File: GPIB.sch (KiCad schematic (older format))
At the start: 22 parts

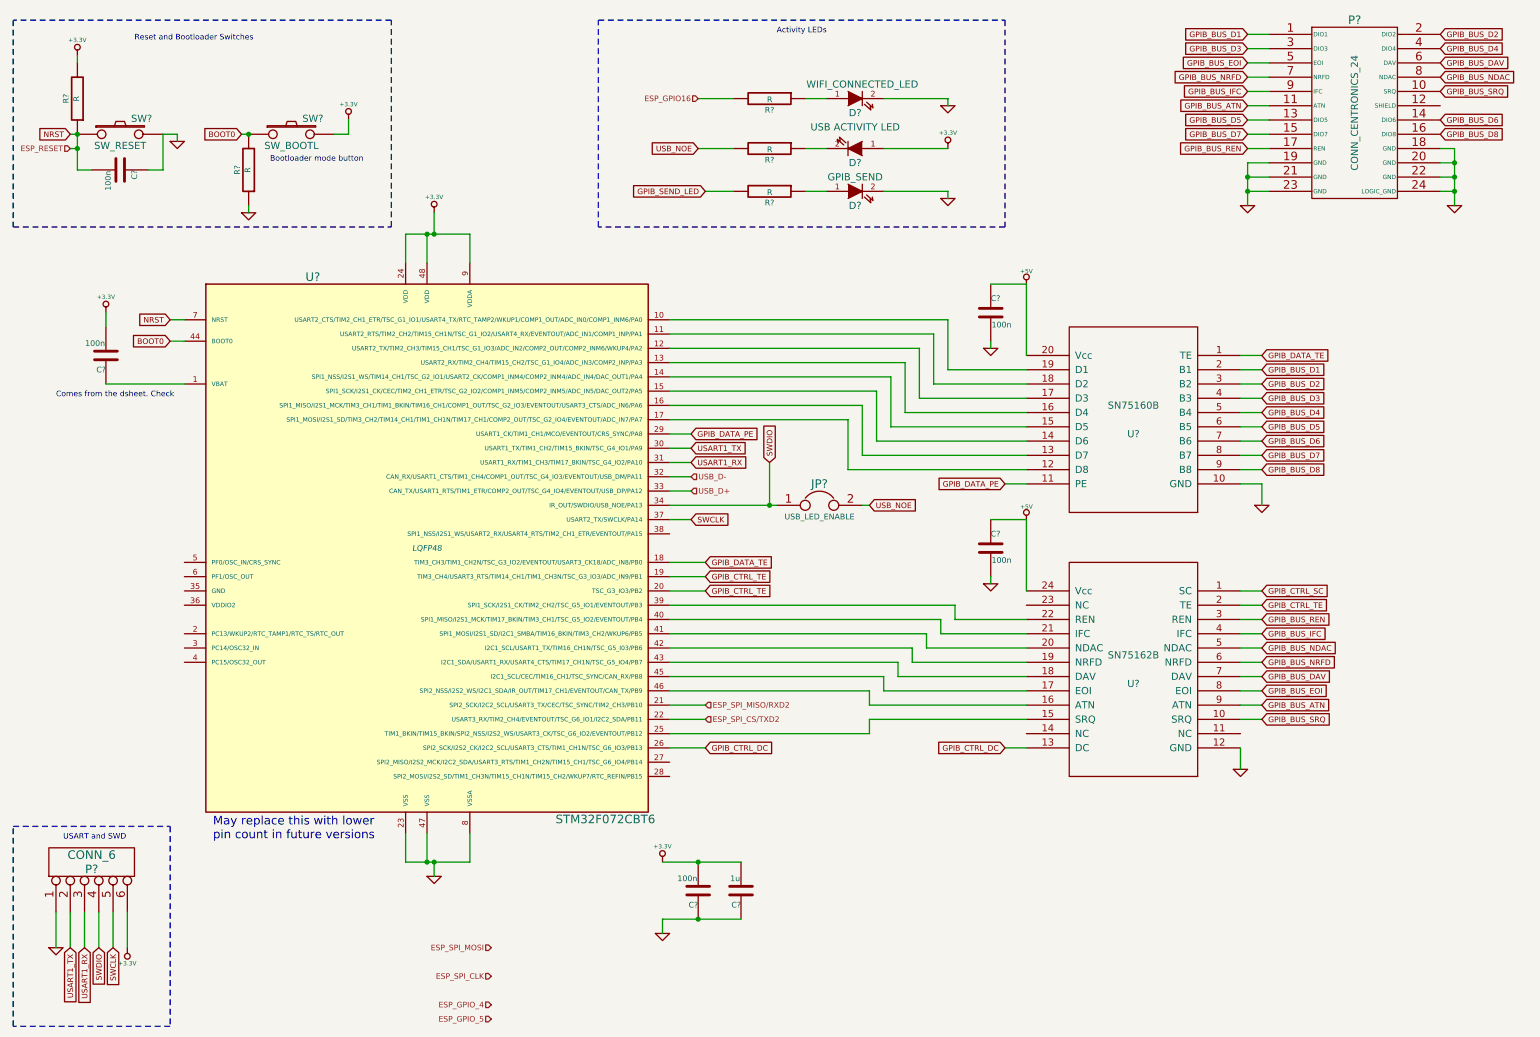
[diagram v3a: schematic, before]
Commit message: ESP doesn't seem to support UART2, switch to UART1
As far as I can tell the TXD2, RXD2 ports are not documented
If they do work, they will only work exclusively of TX1/RX1.
So better to just use the main UART.
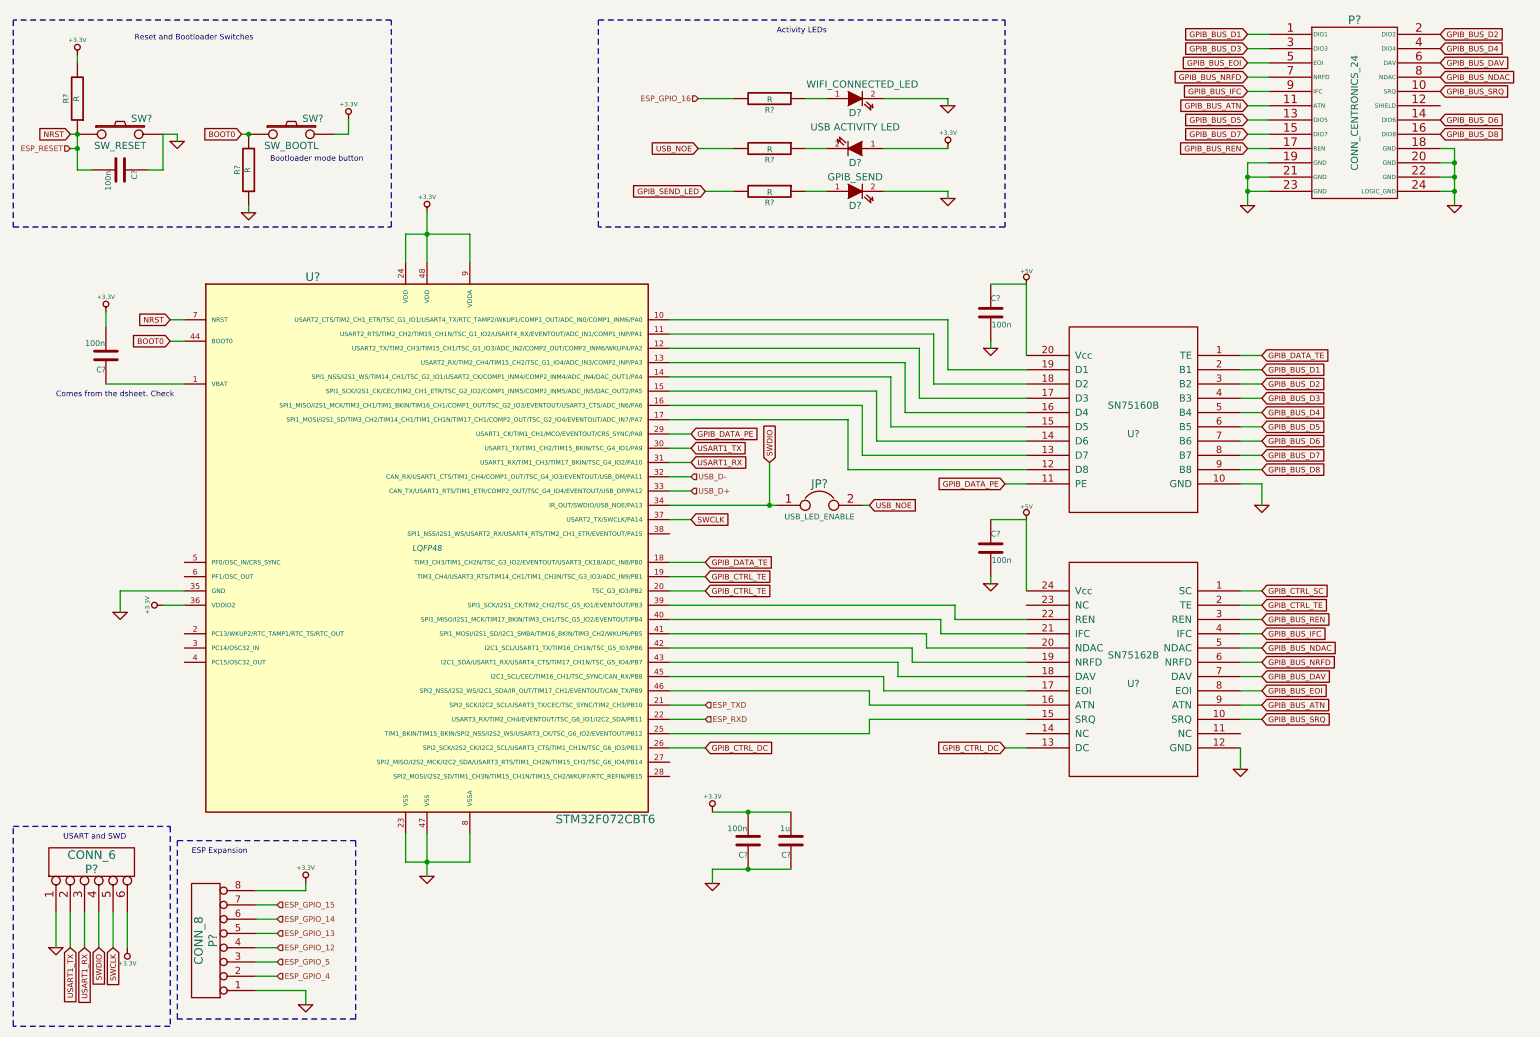
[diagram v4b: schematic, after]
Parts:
- added P?: CONN_8, symbol CONN_8
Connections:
- net +3.3V: now also U?.36 (VDDIO2), P?.8 (P8)
- net ESP_GPIO_4: now also P?.2 (P2)
- net ESP_GPIO_5: now also P?.3 (P3)
- net GND: now also U?.35 (GND), P?.1 (P1)
- net ESP_GPIO16 renamed ESP_GPIO_16
- net ESP_SPI_CS/TXD2 renamed ESP_RXD
- net ESP_SPI_MISO/RXD2 renamed ESP_TXD
- new net ESP_GPIO_12: P?.4 (P4)
- new net ESP_GPIO_13: P?.5 (P5)
- new net ESP_GPIO_14: P?.6 (P6)
- new net ESP_GPIO_15: P?.7 (P7)
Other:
- note added: "ESP Expansion\n"
- note removed: "May replace this with lower\npin count in future versions"
- moved on the sheet: C?
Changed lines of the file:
@@
 	1    0    0    -1
 $EndComp
-Text Notes 2050 6400 0    60   ~ 0
-May replace this with lower\npin count in future versions
 $Comp
 L STM32F072CBT6 U?
@@
 $EndComp
 Wire Wire Line
-	5250 4050 5950 4050
-Wire Wire Line
-	5950 4050 6000 4050
+	5250 4050 6000 4050
 Wire Wire Line
 	5250 3950 5400 3950
@@
 	10650 1550 10750 1550
 Wire Wire Line
-	10750 1550 10750 1650
-Wire Wire Line
-	10750 1650 10750 1750
-Wire Wire Line
-	10750 1750 10750 1850
-Wire Wire Line
-	10750 1850 10750 1950
+	10750 1550 10750 1950
 Wire Wire Line
 	10650 1850 10750 1850
@@
 $EndComp
 Wire Wire Line
-	9300 1650 9300 1750
-Wire Wire Line
-	9300 1750 9300 1850
-Wire Wire Line
-	9300 1850 9300 1950
+	9300 1650 9300 1950
 Connection ~ 9300 1750
 Connection ~ 9300 1850
@@
 Connection ~ 1100 1450
 Wire Wire Line
-	1100 1450 1100 1550
-Wire Wire Line
-	1100 1550 1100 1700
+	1100 1450 1100 1700
 Wire Wire Line
 	1100 1700 1200 1700
@@
 Wire Wire Line
 	1300 3200 1850 3200
-Text HLabel 5500 5550 2    39   Input ~ 0
-ESP_SPI_CS/TXD2
-Text HLabel 4000 7150 0    39   Input ~ 0
-ESP_SPI_MOSI
-Text HLabel 5500 5450 2    39   Input ~ 0
-ESP_SPI_MISO/RXD2
-Text HLabel 4000 7350 0    39   Input ~ 0
-ESP_SPI_CLK
-Text HLabel 4000 7550 0    39   Input ~ 0
+Text HLabel 2500 7350 2    39   Input ~ 0
 ESP_GPIO_4
-Text HLabel 4000 7650 0    39   Input ~ 0
+Text HLabel 2500 7250 2    39   Input ~ 0
 ESP_GPIO_5
 Wire Wire Line
@@
 L +3.3V #PWR?
 U 1 1 556A2965
-P 3600 2000
-F 0 "#PWR?" H 3600 1960 30  0001 C CNN
-F 1 "+3.3V" H 3600 2110 30  0000 C CNN
-F 2 "" H 3600 2000 60  0000 C CNN
-F 3 "" H 3600 2000 60  0000 C CNN
-	1    3600 2000
+P 3550 2000
+F 0 "#PWR?" H 3550 1960 30  0001 C CNN
+F 1 "+3.3V" H 3550 2110 30  0000 C CNN
+F 2 "" H 3550 2000 60  0000 C CNN
+F 3 "" H 3550 2000 60  0000 C CNN
+	1    3550 2000
 	1    0    0    -1
 $EndComp
@@
 	3400 2350 3400 2150
 Wire Wire Line
-	3400 2150 3550 2150
-Wire Wire Line
-	3550 2150 3600 2150
-Wire Wire Line
-	3600 2150 3850 2150
-Wire Wire Line
-	3600 2150 3600 2000
+	3400 2150 3850 2150
+Wire Wire Line
+	3550 2000 3550 2350
 Wire Wire Line
 	3850 2150 3850 2350
-Connection ~ 3600 2150
-Wire Wire Line
-	3550 2350 3550 2150
 Connection ~ 3550 2150
 $Comp
 L +3.3V #PWR?
 U 1 1 556A2C71
-P 5200 6550
-F 0 "#PWR?" H 5200 6510 30  0001 C CNN
-F 1 "+3.3V" H 5200 6660 30  0000 C CNN
-F 2 "" H 5200 6550 60  0000 C CNN
-F 3 "" H 5200 6550 60  0000 C CNN
-	1    5200 6550
+P 5550 6200
+F 0 "#PWR?" H 5550 6160 30  0001 C CNN
+F 1 "+3.3V" H 5550 6310 30  0000 C CNN
+F 2 "" H 5550 6200 60  0000 C CNN
+F 3 "" H 5550 6200 60  0000 C CNN
+	1    5550 6200
 	1    0    0    -1
 $EndComp
@@
 L C C?
 U 1 1 556A2CAC
-P 5450 6750
-F 0 "C?" H 5450 6850 40  0000 L CNN
-F 1 "100n" H 5456 6665 40  0000 L CNN
-F 2 "" H 5488 6600 30  0000 C CNN
-F 3 "" H 5450 6750 60  0000 C CNN
-	1    5450 6750
+P 5800 6400
+F 0 "C?" H 5800 6500 40  0000 L CNN
+F 1 "100n" H 5806 6315 40  0000 L CNN
+F 2 "" H 5838 6250 30  0000 C CNN
+F 3 "" H 5800 6400 60  0000 C CNN
+	1    5800 6400
 	-1   0    0    1
 $EndComp
@@
 L GND #PWR?
 U 1 1 556A2E45
-P 5200 7050
-F 0 "#PWR?" H 5200 7050 30  0001 C CNN
-F 1 "GND" H 5200 6980 30  0001 C CNN
-F 2 "" H 5200 7050 60  0000 C CNN
-F 3 "" H 5200 7050 60  0000 C CNN
-	1    5200 7050
+P 5550 6700
+F 0 "#PWR?" H 5550 6700 30  0001 C CNN
+F 1 "GND" H 5550 6630 30  0001 C CNN
+F 2 "" H 5550 6700 60  0000 C CNN
+F 3 "" H 5550 6700 60  0000 C CNN
+	1    5550 6700
 	1    0    0    -1
 $EndComp
@@
 L C C?
 U 1 1 556A2E72
-P 5750 6750
-F 0 "C?" H 5750 6850 40  0000 L CNN
-F 1 "1u" H 5756 6665 40  0000 L CNN
-F 2 "" H 5788 6600 30  0000 C CNN
-F 3 "" H 5750 6750 60  0000 C CNN
-	1    5750 6750
+P 6100 6400
+F 0 "C?" H 6100 6500 40  0000 L CNN
+F 1 "1u" H 6106 6315 40  0000 L CNN
+F 2 "" H 6138 6250 30  0000 C CNN
+F 3 "" H 6100 6400 60  0000 C CNN
+	1    6100 6400
 	-1   0    0    1
 $EndComp
 Wire Wire Line
-	5200 7050 5200 6950
-Wire Wire Line
-	5200 6950 5450 6950
-Wire Wire Line
-	5450 6950 5750 6950
-Connection ~ 5450 6950
-Wire Wire Line
-	5200 6550 5450 6550
-Wire Wire Line
-	5450 6550 5750 6550
-Connection ~ 5450 6550
+	5550 6700 5550 6600
+Wire Wire Line
+	5550 6600 6100 6600
+Connection ~ 5800 6600
+Wire Wire Line
+	5550 6200 6100 6200
+Connection ~ 5800 6200
 $Comp
 L GND #PWR?
 U 1 1 556A335E
-P 3600 6650
-F 0 "#PWR?" H 3600 6650 30  0001 C CNN
-F 1 "GND" H 3600 6580 30  0001 C CNN
-F 2 "" H 3600 6650 60  0000 C CNN
-F 3 "" H 3600 6650 60  0000 C CNN
-	1    3600 6650
+P 3550 6650
+F 0 "#PWR?" H 3550 6650 30  0001 C CNN
+F 1 "GND" H 3550 6580 30  0001 C CNN
+F 2 "" H 3550 6650 60  0000 C CNN
+F 3 "" H 3550 6650 60  0000 C CNN
+	1    3550 6650
 	1    0    0    -1
 $EndComp
@@
 	3400 6350 3400 6550
 Wire Wire Line
-	3400 6550 3550 6550
-Wire Wire Line
-	3550 6550 3600 6550
-Wire Wire Line
-	3600 6550 3850 6550
-Wire Wire Line
-	3600 6550 3600 6650
+	3400 6550 3850 6550
+Wire Wire Line
+	3550 6350 3550 6650
 Wire Wire Line
 	3850 6550 3850 6350
-Connection ~ 3600 6550
-Wire Wire Line
-	3550 6350 3550 6550
 Connection ~ 3550 6550
 $Comp
@@
 	7200 1200 7200 1250
 Text HLabel 5450 1200 0    39   Input ~ 0
-ESP_GPIO16
+ESP_GPIO_16
 Wire Wire Line
 	5250 5450 5500 5450
@@
 Wire Wire Line
 	5250 5750 5500 5750
+Text HLabel 2500 7150 2    39   Input ~ 0
+ESP_GPIO_12
+Text HLabel 2500 7050 2    39   Input ~ 0
+ESP_GPIO_13
+Text HLabel 2500 6950 2    39   Input ~ 0
+ESP_GPIO_14
+Text HLabel 2500 6850 2    39   Input ~ 0
+ESP_GPIO_15
+Text HLabel 5500 5450 2    39   Input ~ 0
+ESP_TXD
+Text HLabel 5500 5550 2    39   Input ~ 0
+ESP_RXD
+Wire Wire Line
+	1400 4650 1850 4650
+Wire Wire Line
+	1850 4750 1700 4750
+$Comp
+L GND #PWR?
+U 1 1 556BAB4A
+P 1400 4800
+F 0 "#PWR?" H 1400 4800 30  0001 C CNN
+F 1 "GND" H 1400 4730 30  0001 C CNN
+F 2 "" H 1400 4800 60  0000 C CNN
+F 3 "" H 1400 4800 60  0000 C CNN
+	1    1400 4800
+	1    0    0    -1
+$EndComp
+$Comp
+L +3.3V #PWR?
+U 1 1 556BADA7
+P 1700 4750
+F 0 "#PWR?" H 1700 4710 30  0001 C CNN
+F 1 "+3.3V" H 1700 4860 30  0000 C CNN
+F 2 "" H 1700 4750 60  0000 C CNN
+F 3 "" H 1700 4750 60  0000 C CNN
+	1    1700 4750
+	0    -1   -1   0
+$EndComp
+Wire Wire Line
+	1400 4650 1400 4800
+$Comp
+L CONN_8 P?
+U 1 1 556BB559
+P 2000 7100
+F 0 "P?" V 1950 7100 60  0000 C CNN
+F 1 "CONN_8" V 2050 7100 60  0000 C CNN
+F 2 "" H 2000 7100 60  0000 C CNN
+F 3 "" H 2000 7100 60  0000 C CNN
+	1    2000 7100
+	-1   0    0    1
+$EndComp
+Wire Wire Line
+	2350 7450 2700 7450
+Wire Wire Line
+	2350 7350 2500 7350
+Wire Wire Line
+	2350 7250 2500 7250
+Wire Wire Line
+	2350 7150 2500 7150
+Wire Wire Line
+	2350 7050 2500 7050
+Wire Wire Line
+	2350 6950 2500 6950
+Wire Wire Line
+	2350 6850 2500 6850
+$Comp
+L GND #PWR?
+U 1 1 556BBE46
+P 2700 7550
+F 0 "#PWR?" H 2700 7550 30  0001 C CNN
+F 1 "GND" H 2700 7480 30  0001 C CNN
+F 2 "" H 2700 7550 60  0000 C CNN
+F 3 "" H 2700 7550 60  0000 C CNN
+	1    2700 7550
+	1    0    0    -1
+$EndComp
+$Comp
+L +3.3V #PWR?
+U 1 1 556BBE7F
+P 2700 6700
+F 0 "#PWR?" H 2700 6660 30  0001 C CNN
+F 1 "+3.3V" H 2700 6810 30  0000 C CNN
+F 2 "" H 2700 6700 60  0000 C CNN
+F 3 "" H 2700 6700 60  0000 C CNN
+	1    2700 6700
+	1    0    0    -1
+$EndComp
+Wire Wire Line
+	2350 6750 2700 6750
+Wire Wire Line
+	2700 6750 2700 6700
+Wire Wire Line
+	2700 7450 2700 7550
+Wire Notes Line
+	1800 6400 3050 6400
+Wire Notes Line
+	3050 6400 3050 7650
+Wire Notes Line
+	3050 7650 1800 7650
+Wire Notes Line
+	1800 7650 1800 6400
+Text Notes 1900 6500 0    39   ~ 0
+ESP Expansion\n
 $EndSCHEMATC

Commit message: Add rst to debug conn
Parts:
- removed P?: CONN_6, symbol CONN_6
- added P?: CONN_8, symbol CONN_8
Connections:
- net +3.3V: now also P?.8 (P8)
- net GND: now also P?.1 (P1)
- net NRST: now also P?.6 (P6)
- net SWCLK: now also P?.5 (P5)
- net SWDIO: now also P?.4 (P4)
- net USART1_RX: now also P?.3 (P3)
- net USART1_TX: now also P?.2 (P2)
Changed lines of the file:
@@
 	5250 3750 5400 3750
-$Comp
-L CONN_6 P?
-U 1 1 556A65EF
-P 1200 6550
-F 0 "P?" V 1150 6550 60  0000 C CNN
-F 1 "CONN_6" V 1250 6550 60  0000 C CNN
-F 2 "" H 1200 6550 60  0000 C CNN
-F 3 "" H 1200 6550 60  0000 C CNN
-	1    1200 6550
-	0    -1   -1   0
-$EndComp
 $Comp
 L GND #PWR?
@@
 L +3.3V #PWR?
 U 1 1 556A68A8
-P 1450 7150
-F 0 "#PWR?" H 1450 7110 30  0001 C CNN
-F 1 "+3.3V" H 1450 7260 30  0000 C CNN
-F 2 "" H 1450 7150 60  0000 C CNN
-F 3 "" H 1450 7150 60  0000 C CNN
-	1    1450 7150
+P 1650 7150
+F 0 "#PWR?" H 1650 7110 30  0001 C CNN
+F 1 "+3.3V" H 1650 7260 30  0000 C CNN
+F 2 "" H 1650 7150 60  0000 C CNN
+F 3 "" H 1650 7150 60  0000 C CNN
+	1    1650 7150
 	-1   0    0    1
 $EndComp
 Wire Wire Line
 	950  6900 950  7150
-Wire Wire Line
-	1450 6900 1450 7150
 Wire Wire Line
 	1050 6900 1050 7150
@@
 Text Notes 1900 6500 0    39   ~ 0
 ESP Expansion\n
+$Comp
+L CONN_8 P?
+U 1 1 556BDE74
+P 1300 6550
+F 0 "P?" V 1250 6550 60  0000 C CNN
+F 1 "CONN_8" V 1350 6550 60  0000 C CNN
+F 2 "" H 1300 6550 60  0000 C CNN
+F 3 "" H 1300 6550 60  0000 C CNN
+	1    1300 6550
+	0    -1   -1   0
+$EndComp
+Wire Wire Line
+	1650 6900 1650 7150
+Wire Wire Line
+	1450 6900 1450 7150
+Text GLabel 1450 7150 3    39   Input ~ 0
+NRST
 $EndSCHEMATC

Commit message: Use ST-Link (standard?) header
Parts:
- removed P?: CONN_8, symbol CONN_8
- added P?: CONN_6, symbol CONN_6
- added P?: CONN_2, symbol CONN_2
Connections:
- net +3.3V: now also P?.1
- net GND: now also P?.3
- net NRST: now also P?.5
- net SWCLK: now also P?.2
- net SWDIO: now also P?.4
- net USART1_RX: now also P?.2 (PM)
- net USART1_TX: now also P?.1 (P1)
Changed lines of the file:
@@
 L GND #PWR?
 U 1 1 556A686C
+P 1150 7150
+F 0 "#PWR?" H 1150 7150 30  0001 C CNN
+F 1 "GND" H 1150 7080 30  0001 C CNN
+F 2 "" H 1150 7150 60  0000 C CNN
+F 3 "" H 1150 7150 60  0000 C CNN
+	1    1150 7150
+	1    0    0    -1
+$EndComp
+$Comp
+L +3.3V #PWR?
+U 1 1 556A68A8
 P 950 7150
-F 0 "#PWR?" H 950 7150 30  0001 C CNN
-F 1 "GND" H 950 7080 30  0001 C CNN
+F 0 "#PWR?" H 950 7110 30  0001 C CNN
+F 1 "+3.3V" H 950 7260 30  0000 C CNN
 F 2 "" H 950 7150 60  0000 C CNN
 F 3 "" H 950 7150 60  0000 C CNN
 	1    950  7150
-	1    0    0    -1
-$EndComp
-$Comp
-L +3.3V #PWR?
-U 1 1 556A68A8
-P 1650 7150
-F 0 "#PWR?" H 1650 7110 30  0001 C CNN
-F 1 "+3.3V" H 1650 7260 30  0000 C CNN
-F 2 "" H 1650 7150 60  0000 C CNN
-F 3 "" H 1650 7150 60  0000 C CNN
-	1    1650 7150
 	-1   0    0    1
 $EndComp
@@
 Wire Wire Line
 	1050 6900 1050 7150
-Text GLabel 1050 7150 3    39   Input ~ 0
+Text GLabel 1150 6000 3    39   Input ~ 0
 USART1_TX
-Text GLabel 1150 7150 3    39   Input ~ 0
+Text GLabel 1350 6000 3    39   Input ~ 0
 USART1_RX
 Text GLabel 1250 7150 3    39   Input ~ 0
 SWDIO
-Text GLabel 1350 7150 3    39   Input ~ 0
+Text GLabel 1050 7150 3    39   Input ~ 0
 SWCLK
 Wire Wire Line
@@
 	1150 6900 1150 7150
 Wire Notes Line
-	650  6300 1750 6300
-Wire Notes Line
-	1750 6300 1750 7700
+	1750 5250 1750 7700
 Wire Notes Line
 	1750 7700 650  7700
 Wire Notes Line
-	650  7700 650  6300
-Text Notes 1000 6400 0    39   ~ 0
+	650  7700 650  5250
+Text Notes 1050 5400 0    39   ~ 0
 USART and SWD
 Wire Notes Line
@@
 Text Notes 1900 6500 0    39   ~ 0
 ESP Expansion\n
-$Comp
-L CONN_8 P?
-U 1 1 556BDE74
-P 1300 6550
-F 0 "P?" V 1250 6550 60  0000 C CNN
-F 1 "CONN_8" V 1350 6550 60  0000 C CNN
-F 2 "" H 1300 6550 60  0000 C CNN
-F 3 "" H 1300 6550 60  0000 C CNN
-	1    1300 6550
+Text GLabel 1350 7150 3    39   Input ~ 0
+NRST
+$Comp
+L CONN_6 P?
+U 1 1 556BF93D
+P 1200 6550
+F 0 "P?" V 1150 6550 60  0000 C CNN
+F 1 "CONN_6" V 1250 6550 60  0000 C CNN
+F 2 "" H 1200 6550 60  0000 C CNN
+F 3 "" H 1200 6550 60  0000 C CNN
+	1    1200 6550
 	0    -1   -1   0
 $EndComp
-Wire Wire Line
-	1650 6900 1650 7150
-Wire Wire Line
-	1450 6900 1450 7150
-Text GLabel 1450 7150 3    39   Input ~ 0
-NRST
+$Comp
+L CONN_2 P?
+U 1 1 556BFBCD
+P 1250 5550
+F 0 "P?" V 1200 5550 40  0000 C CNN
+F 1 "CONN_2" V 1300 5550 40  0000 C CNN
+F 2 "" H 1250 5550 60  0000 C CNN
+F 3 "" H 1250 5550 60  0000 C CNN
+	1    1250 5550
+	0    -1   -1   0
+$EndComp
+Wire Wire Line
+	1350 6000 1350 5900
+Wire Wire Line
+	1150 6000 1150 5900
+Wire Notes Line
+	650  5250 1750 5250
 $EndSCHEMATC

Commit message: DRCs mostly fixed
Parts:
- gave numbers to parts that had none: 24
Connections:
- net GPIB_CTRL_SC: now also U5.27 (SPI2_MISO/I2S2_MCK/I2C2_SDA/USART3_RTS/TIM1_CH2N/TIM15_CH1/TSC_G6_IO4/PB14)
- net GPIB_SEND_LED: now also U5.28 (SPI2_MOSI/I2S2_SD/TIM1_CH3N/TIM15_CH1N/TIM15_CH2/WKUP7/RTC_REFIN/PB15)
